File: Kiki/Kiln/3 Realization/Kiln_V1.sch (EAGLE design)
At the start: 19 parts, among them T1 2N3904, T2 2N3904, T3 2N3904, T4 2N3904

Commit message: Updated: 3.3v & GND Disconnected the 3.3v pin -- the was a supply pin, not a power in pin. Attached the GND for the transistors to BOTH Arduino ground pins, and beefec up the trace, just in case.  I wonder if this is enough to dump the transistors, when all segments of the digit are illuminated?
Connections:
- removed net N$30: JP3.8, PCB1.3.3V
- net GND: now also PCB1.GND., PCB1.GND..
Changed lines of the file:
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@@
 <instance part="U$24" gate="G$1" x="43.18" y="58.42"/>
 <instance part="U$25" gate="G$1" x="40.64" y="55.88"/>
-<instance part="GND1" gate="1" x="111.76" y="43.18"/>
+<instance part="GND1" gate="1" x="111.76" y="-7.62"/>
 </instances>
 <busses>
@@
 <wire x1="58.42" y1="53.34" x2="58.42" y2="48.26" width="0.1524" layer="91"/>
 <label x="58.42" y="53.34" size="1.778" layer="95" rot="R90"/>
-</segment>
-</net>
-<net name="N$30" class="0">
-<segment>
-<pinref part="JP3" gate="A" pin="8"/>
-<wire x1="43.18" y1="48.26" x2="43.18" y2="43.18" width="0.4064" layer="91"/>
-<wire x1="43.18" y1="43.18" x2="17.78" y2="43.18" width="0.4064" layer="91"/>
-<wire x1="17.78" y1="43.18" x2="17.78" y2="-12.7" width="0.4064" layer="91"/>
-<wire x1="17.78" y1="-12.7" x2="55.88" y2="-12.7" width="0.4064" layer="91"/>
-<pinref part="PCB1" gate="G$1" pin="3.3V"/>
-<wire x1="55.88" y1="-12.7" x2="55.88" y2="-5.08" width="0.4064" layer="91"/>
 </segment>
 </net>
@@
 <junction x="137.16" y="48.26"/>
 <junction x="144.78" y="48.26"/>
-<wire x1="111.76" y1="48.26" x2="111.76" y2="45.72" width="0.4064" layer="91"/>
+<wire x1="111.76" y1="48.26" x2="111.76" y2="0" width="0.4064" layer="91"/>
 <pinref part="GND1" gate="1" pin="GND"/>
-</segment>
-</net>
+<pinref part="PCB1" gate="G$1" pin="GND."/>
+<wire x1="111.76" y1="0" x2="111.76" y2="-2.54" width="0.4064" layer="91"/>
+<wire x1="111.76" y1="-2.54" x2="111.76" y2="-5.08" width="0.4064" layer="91"/>
+<wire x1="63.5" y1="-5.08" x2="63.5" y2="-17.78" width="0.4064" layer="91"/>
+<wire x1="63.5" y1="-17.78" x2="116.84" y2="-17.78" width="0.4064" layer="91"/>
+<wire x1="116.84" y1="-17.78" x2="116.84" y2="-2.54" width="0.4064" layer="91"/>
+<wire x1="116.84" y1="-2.54" x2="111.76" y2="-2.54" width="0.4064" layer="91"/>
+<pinref part="PCB1" gate="G$1" pin="GND.."/>
+<wire x1="60.96" y1="-5.08" x2="60.96" y2="-20.32" width="0.4064" layer="91"/>
+<wire x1="60.96" y1="-20.32" x2="119.38" y2="-20.32" width="0.4064" layer="91"/>
+<wire x1="119.38" y1="-20.32" x2="119.38" y2="0" width="0.4064" layer="91"/>
+<wire x1="119.38" y1="0" x2="111.76" y2="0" width="0.4064" layer="91"/>
+<junction x="111.76" y="-2.54"/>
+<junction x="111.76" y="0"/>
+</segment>
+</net>

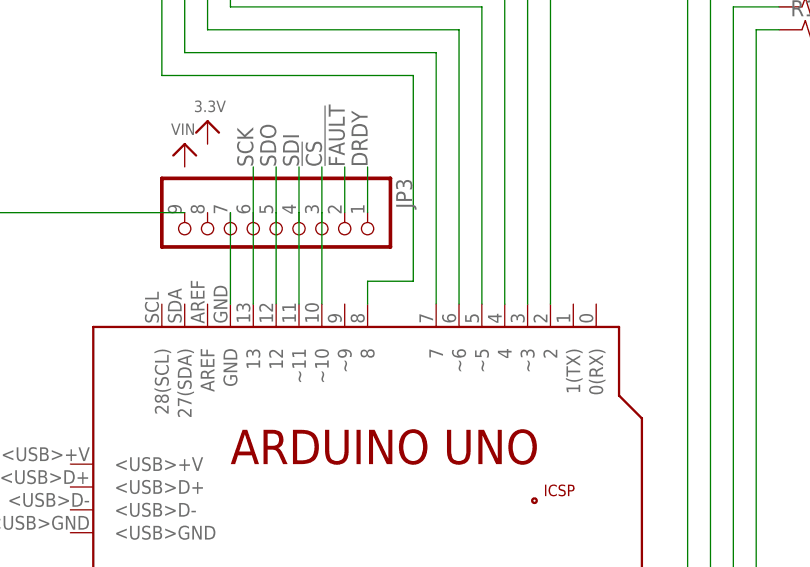
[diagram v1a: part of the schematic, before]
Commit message: Update: minor changes Changed the name of the Thermal Amplifier JP3 connector, for clarity.
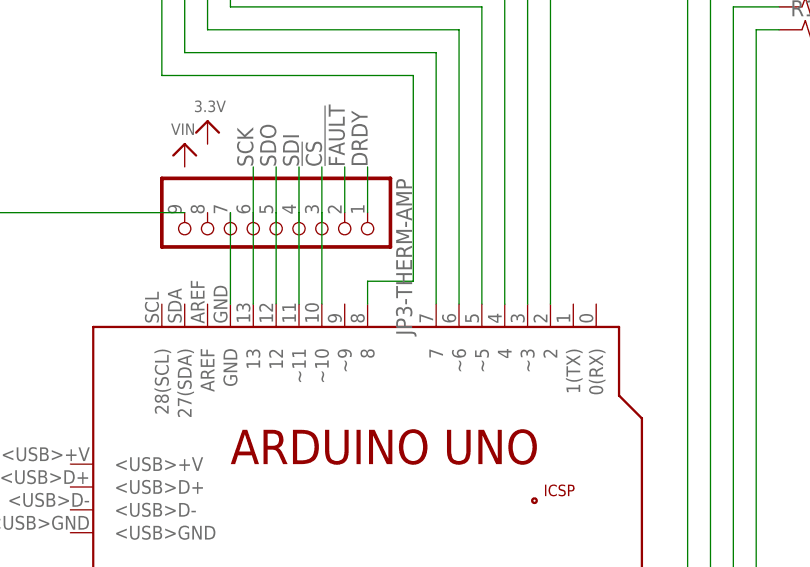
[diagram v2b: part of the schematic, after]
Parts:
- renumbered JP3 to JP3-THERM-AMP
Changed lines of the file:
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@@
 <part name="T3" library="transistor" deviceset="2N3904" device=""/>
 <part name="T4" library="transistor" deviceset="2N3904" device=""/>
-<part name="JP3" library="microbuilder" deviceset="HEADER-1X9" device="70MIL"/>
+<part name="JP3-THERM-AMP" library="microbuilder" deviceset="HEADER-1X9" device="70MIL"/>
 <part name="U$24" library="microbuilder" deviceset="3.3V" device=""/>
 <part name="U$25" library="microbuilder" deviceset="VIN" device=""/>
@@
 <attribute name="VALUE" x="157.48" y="53.34" size="1.778" layer="96"/>
 </instance>
-<instance part="JP3" gate="A" x="50.8" y="45.72" smashed="yes" rot="R270">
+<instance part="JP3-THERM-AMP" gate="A" x="50.8" y="45.72" smashed="yes" rot="R270">
 <attribute name="NAME" x="64.135" y="52.07" size="1.778" layer="95" rot="R270"/>
 <attribute name="VALUE" x="35.56" y="52.07" size="1.778" layer="96" rot="R270"/>
@@
 <net name="DRDY" class="0">
 <segment>
-<pinref part="JP3" gate="A" pin="1"/>
+<pinref part="JP3-THERM-AMP" gate="A" pin="1"/>
 <wire x1="60.96" y1="48.26" x2="60.96" y2="53.34" width="0.1524" layer="91"/>
 <label x="60.96" y="53.34" size="1.778" layer="95" rot="R90"/>
@@
 <net name="SCK" class="0">
 <segment>
-<pinref part="JP3" gate="A" pin="6"/>
+<pinref part="JP3-THERM-AMP" gate="A" pin="6"/>
 <wire x1="48.26" y1="53.34" x2="48.26" y2="48.26" width="0.1524" layer="91"/>
 <label x="48.26" y="53.34" size="1.778" layer="95" rot="R90"/>
@@
 <segment>
 <wire x1="50.8" y1="53.34" x2="50.8" y2="48.26" width="0.1524" layer="91"/>
-<pinref part="JP3" gate="A" pin="5"/>
+<pinref part="JP3-THERM-AMP" gate="A" pin="5"/>
 <label x="50.8" y="53.34" size="1.778" layer="95" rot="R90"/>
 <pinref part="PCB1" gate="G$1" pin="12"/>
@@
 <segment>
 <wire x1="53.34" y1="53.34" x2="53.34" y2="48.26" width="0.1524" layer="91"/>
-<pinref part="JP3" gate="A" pin="4"/>
+<pinref part="JP3-THERM-AMP" gate="A" pin="4"/>
 <label x="53.34" y="53.34" size="1.778" layer="95" rot="R90"/>
 <pinref part="PCB1" gate="G$1" pin="~11"/>
@@
 <segment>
 <wire x1="55.88" y1="53.34" x2="55.88" y2="48.26" width="0.1524" layer="91"/>
-<pinref part="JP3" gate="A" pin="3"/>
+<pinref part="JP3-THERM-AMP" gate="A" pin="3"/>
 <label x="55.88" y="53.34" size="1.778" layer="95" rot="R90"/>
 <pinref part="PCB1" gate="G$1" pin="~10"/>
@@
 <net name="!FAULT" class="0">
 <segment>
-<pinref part="JP3" gate="A" pin="2"/>
+<pinref part="JP3-THERM-AMP" gate="A" pin="2"/>
 <wire x1="58.42" y1="53.34" x2="58.42" y2="48.26" width="0.1524" layer="91"/>
 <label x="58.42" y="53.34" size="1.778" layer="95" rot="R90"/>
@@
 <net name="N$31" class="0">
 <segment>
-<pinref part="JP3" gate="A" pin="9"/>
+<pinref part="JP3-THERM-AMP" gate="A" pin="9"/>
 <wire x1="40.64" y1="48.26" x2="15.24" y2="48.26" width="0.4064" layer="91"/>
 <wire x1="15.24" y1="48.26" x2="15.24" y2="-15.24" width="0.4064" layer="91"/>
@@
 <segment>
 <pinref part="PCB1" gate="G$1" pin="GND"/>
-<pinref part="JP3" gate="A" pin="7"/>
+<pinref part="JP3-THERM-AMP" gate="A" pin="7"/>
 <wire x1="45.72" y1="38.1" x2="45.72" y2="48.26" width="0.4064" layer="91"/>
 </segment>

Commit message: Update: new display The display file was the wrong size.  Rebuilt it. Layout got horked, so had to rebuild it from scratch. Also added the relay and Heating indicator light.
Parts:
- removed 4DIG_7SEG1: (no value), 7-seg-disp:4DIG_7SEG
- added LED1: (no value), 1-Generic:LED3MM
- added R-REPLACE_ME: 0.1OHM-1/2W-1%(1210), SparkFun-Resistors:0.1OHM-1/2W-1%(1210)
- added U$1: 4DIG_7SEG_056, 7-seg-disp:4DIG_7SEG_056
- added X1: 3.5mm term, microbuilder:TERMBLOCK_1X2
- R10, R11, R8, R9: value (none) -> 4.7K; device SparkFun-Resistors:4.7OHM-1/10W-5%(0603) -> SparkFun-Resistors:4.7KOHM-1/10W-1%(0603)
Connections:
- removed net !FAULT: JP3-THERM-AMP.2
- removed net DRDY: JP3-THERM-AMP.1
- removed net N$28: JP3-THERM-AMP.7, PCB1.GND
- new net N$21: LED1.A, R-REPLACE_ME.2
- new net RELAY_POS: PCB1.~9, R-REPLACE_ME.1, X1.1
- net GND: now also JP3-THERM-AMP.7, LED1.C, PCB1.GND, X1.2
- net N$10: now also U$1.A; no longer 4DIG_7SEG1.A
- net N$11: now also U$1.B; no longer 4DIG_7SEG1.B
- net N$12: now also U$1.C; no longer 4DIG_7SEG1.C
- net N$13: now also U$1.D; no longer 4DIG_7SEG1.D
- net N$14: now also U$1.E; no longer 4DIG_7SEG1.E
- net N$15: now also U$1.F; no longer 4DIG_7SEG1.F
- net N$16: now also U$1.G; no longer 4DIG_7SEG1.G
- net N$17: now also PCB1.A3; no longer PCB1.A5
- net N$18: now also PCB1.A2; no longer PCB1.A4
- net N$19: now also PCB1.A1; no longer PCB1.A3
- net N$20: now also PCB1.A0; no longer PCB1.A2
- net N$5: now also U$1.DIG4; no longer 4DIG_7SEG1.DIG4
- net N$6: now also U$1.DIG3; no longer 4DIG_7SEG1.DIG3
- net N$7: now also U$1.DIG2; no longer 4DIG_7SEG1.DIG2
- net N$8: now also U$1.DIG1; no longer 4DIG_7SEG1.DIG1

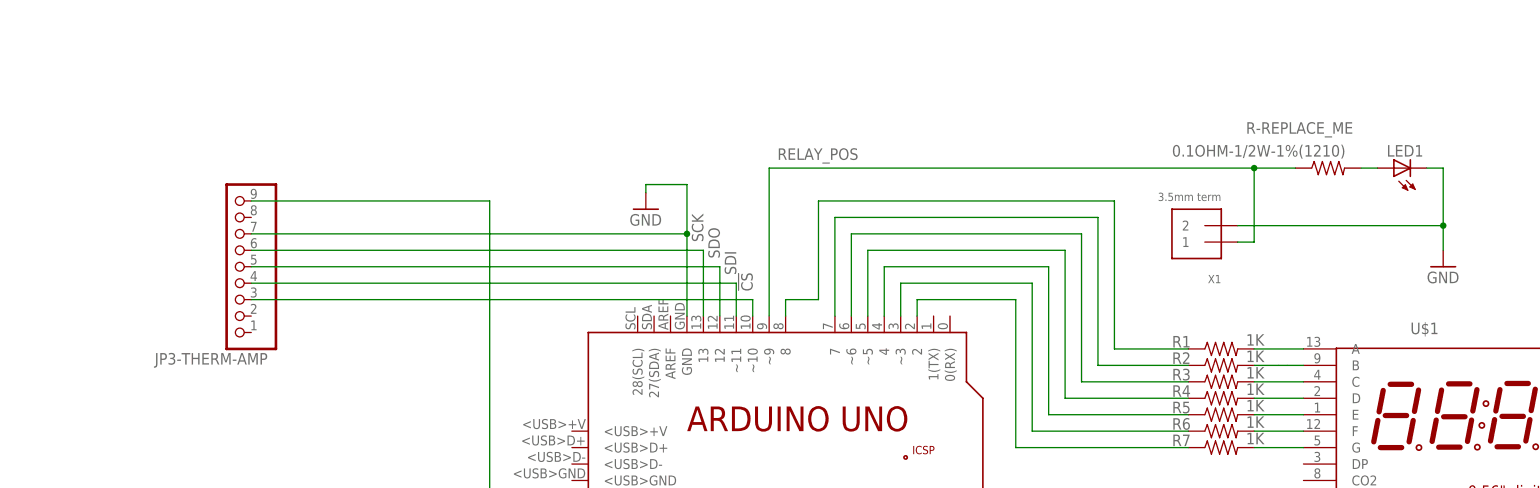
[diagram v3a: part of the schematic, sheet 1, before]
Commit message: Update: changed R12, LED Replaced these with real parts.  Cleared the ERC. But this does not follow proper guidelines.
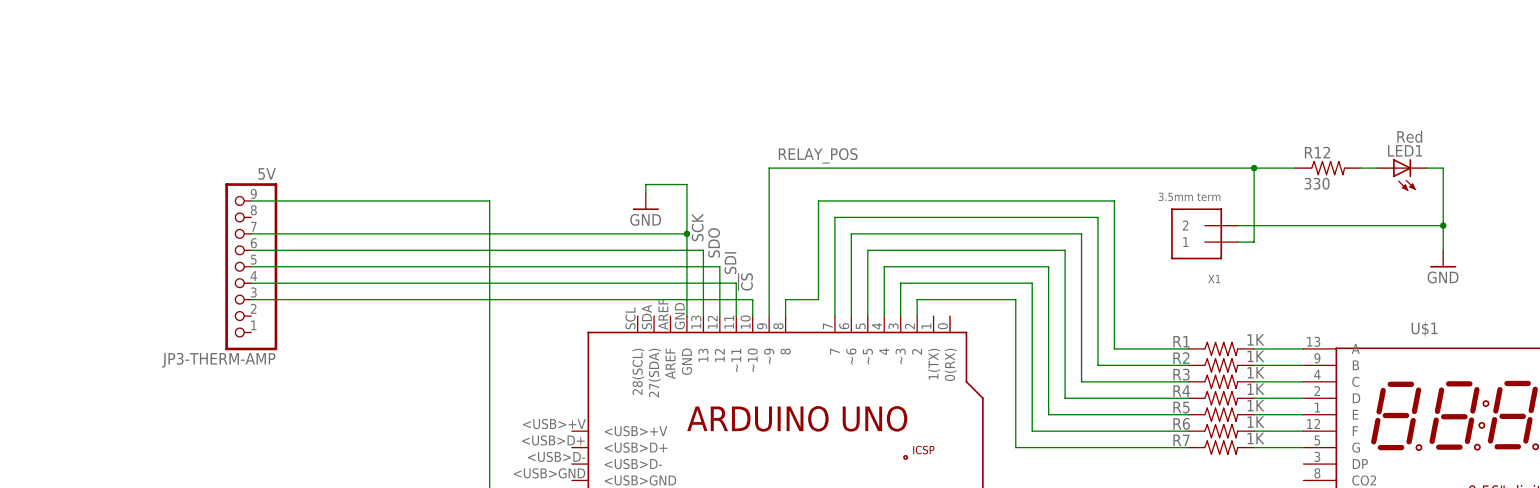
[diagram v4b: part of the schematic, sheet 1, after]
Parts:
- removed R-REPLACE_ME: 0.1OHM-1/2W-1%(1210), SparkFun-Resistors:0.1OHM-1/2W-1%(1210)
- added R12: 330, SparkFun-Resistors:330OHM1/10W1%(0603)
- JP3-THERM-AMP: value (none) -> 5V
- LED1: value (none) -> Red
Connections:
- net N$21: now also R12.2; no longer R-REPLACE_ME.2
- net RELAY_POS: now also R12.1; no longer R-REPLACE_ME.1
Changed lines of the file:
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@@
 <schematic xreflabel="%F%N/%S.%C%R" xrefpart="/%S.%C%R">
 <attributes>
-<attribute name="REV" value="1.0"/>
+<attribute name="REV" value="2.0"/>
 </attributes>
 <variantdefs>
@@
 <part name="T3" library="transistor" deviceset="2N3904" device=""/>
 <part name="T4" library="transistor" deviceset="2N3904" device=""/>
-<part name="JP3-THERM-AMP" library="microbuilder" deviceset="HEADER-1X9" device="70MIL"/>
+<part name="JP3-THERM-AMP" library="microbuilder" deviceset="HEADER-1X9" device="70MIL" value="5V"/>
 <part name="GND2" library="supply1" deviceset="GND" device=""/>
 <part name="GND3" library="supply1" deviceset="GND" device=""/>
@@
 <part name="R11" library="SparkFun-Resistors" deviceset="4.7KOHM-1/10W-1%(0603)" device="" value="4.7K"/>
 <part name="U$1" library="7-seg-disp" deviceset="4DIG_7SEG_056" device=""/>
-<part name="LED1" library="1-Generic" deviceset="LED" device="3MM"/>
-<part name="R-REPLACE_ME" library="SparkFun-Resistors" deviceset="0.1OHM-1/2W-1%(1210)" device=""/>
+<part name="LED1" library="1-Generic" deviceset="LED" device="3MM" value="Red"/>
 <part name="X1" library="microbuilder" deviceset="TERMBLOCK_1X2" device="" value="3.5mm term"/>
 <part name="GND1" library="supply1" deviceset="GND" device=""/>
+<part name="R12" library="SparkFun-Resistors" deviceset="330OHM1/10W1%(0603)" device="" value="330"/>
 </parts>
 <sheets>
@@
 </instance>
 <instance part="JP3-THERM-AMP" gate="A" x="-24.13" y="45.72" smashed="yes" rot="R180">
-<attribute name="NAME" x="-19.05" y="32.385" size="1.778" layer="95" rot="R180"/>
+<attribute name="NAME" x="-17.78" y="32.385" size="1.778" layer="95" rot="R180"/>
 <attribute name="VALUE" x="-17.78" y="60.96" size="1.778" layer="96" rot="R180"/>
 </instance>
@@
 </instance>
 <instance part="U$1" gate="G$1" x="171.45" y="22.86"/>
-<instance part="LED1" gate="G$1" x="154.94" y="60.96" rot="R90"/>
-<instance part="R-REPLACE_ME" gate="G$1" x="144.78" y="60.96" smashed="yes">
-<attribute name="NAME" x="132.08" y="66.2686" size="1.778" layer="95"/>
-<attribute name="VALUE" x="120.65" y="62.738" size="1.778" layer="96"/>
+<instance part="LED1" gate="G$1" x="154.94" y="60.96" smashed="yes" rot="R90">
+<attribute name="NAME" x="159.512" y="64.516" size="1.778" layer="95" rot="R180"/>
+<attribute name="VALUE" x="159.512" y="66.675" size="1.778" layer="96" rot="R180"/>
 </instance>
 <instance part="X1" gate="G$1" x="125.73" y="52.07" rot="R180"/>
 <instance part="GND1" gate="1" x="162.56" y="45.72"/>
+<instance part="R12" gate="G$1" x="144.78" y="60.96"/>
 </instances>
 <busses>
@@
 <wire x1="58.42" y1="60.96" x2="133.35" y2="60.96" width="0.4064" layer="91"/>
 <label x="59.69" y="62.23" size="1.778" layer="95"/>
-<pinref part="R-REPLACE_ME" gate="G$1" pin="1"/>
-<wire x1="133.35" y1="60.96" x2="139.7" y2="60.96" width="0.4064" layer="91"/>
 <wire x1="133.35" y1="60.96" x2="133.35" y2="49.53" width="0.4064" layer="91"/>
 <pinref part="X1" gate="G$1" pin="1"/>
 <wire x1="133.35" y1="49.53" x2="130.81" y2="49.53" width="0.4064" layer="91"/>
+<pinref part="R12" gate="G$1" pin="1"/>
+<wire x1="133.35" y1="60.96" x2="139.7" y2="60.96" width="0.4064" layer="91"/>
 <junction x="133.35" y="60.96"/>
-</segment>
-</net>
-<net name="N$21" class="0">
-<segment>
-<pinref part="R-REPLACE_ME" gate="G$1" pin="2"/>
-<pinref part="LED1" gate="G$1" pin="A"/>
-<wire x1="149.86" y1="60.96" x2="152.4" y2="60.96" width="0.4064" layer="91"/>
 </segment>
 </net>
@@
 </segment>
 </net>
+<net name="N$21" class="0">
+<segment>
+<pinref part="R12" gate="G$1" pin="2"/>
+<pinref part="LED1" gate="G$1" pin="A"/>
+<wire x1="149.86" y1="60.96" x2="152.4" y2="60.96" width="0.4064" layer="91"/>
+</segment>
+</net>

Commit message: Update: cleared DRC errors Have not fixed the Drill errors, but cleared the main ones.
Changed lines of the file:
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@@
 <schematic xreflabel="%F%N/%S.%C%R" xrefpart="/%S.%C%R">
 <attributes>
+<attribute name="DESIGN" value="Kiki Jewell"/>
 <attribute name="REV" value="2.0"/>
 </attributes>
@@
 <sheet>
 <plain>
+<text x="270.51" y="-66.04" size="1.778" layer="91">&gt;REV</text>
+<text x="201.93" y="-62.23" size="1.778" layer="91">&gt;DESIGN</text>
 </plain>
 <instances>
-<instance part="FRAME1" gate="G$1" x="-152.4" y="-73.66"/>
+<instance part="FRAME1" gate="G$1" x="-152.4" y="-73.66" smashed="yes"/>
 <instance part="FRAME1" gate="G$2" x="177.8" y="-73.66"/>
 <instance part="PCB1" gate="G$1" x="60.96" y="17.78"/>
@@
 </nets>
 </sheet>
-<sheet>
-<plain>
-</plain>
-<instances>
-</instances>
-<busses>
-</busses>
-<nets>
-</nets>
-</sheet>
